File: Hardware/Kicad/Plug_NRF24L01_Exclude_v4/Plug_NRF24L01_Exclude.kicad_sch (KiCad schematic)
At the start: 39 parts, among them J1 Conn_01x07_Socket, J2 Conn_01x08_Socket, J2 Conn_02x07_Odd_Even, Q1 2N7002, Q2 2N7002, Q3 2N7002, SW2 SW_SPST, U2 MIC5219-3.3YMM, U3 STM32L412KBTx

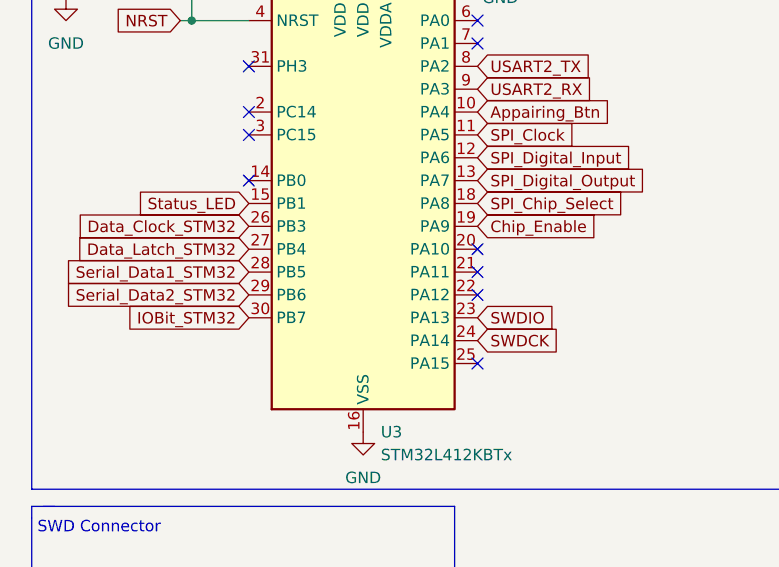
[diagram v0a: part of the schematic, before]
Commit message: Update Plug_NRF24L01_Exclude v4.0a (Schematic Fixes / New PCB Routing) - Added new images
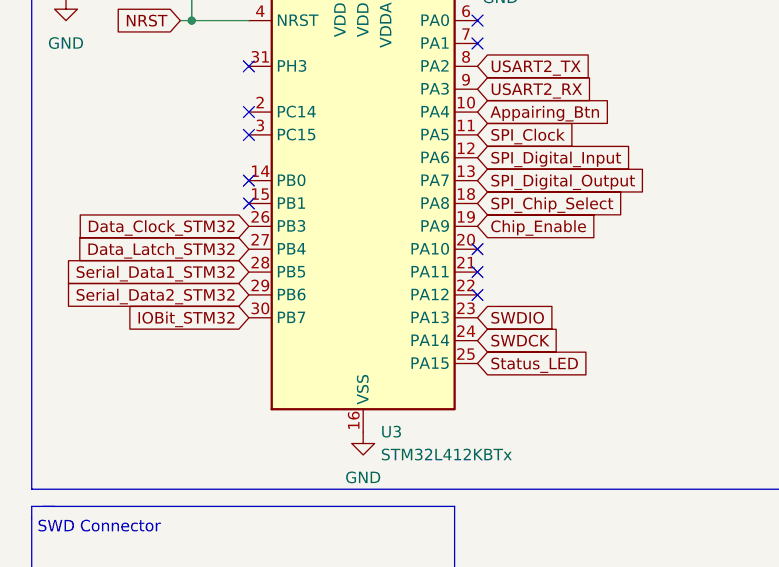
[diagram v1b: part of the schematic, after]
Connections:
- net Status_LED: now also U3.25 (PA15); no longer U3.15 (PB1)
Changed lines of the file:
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@@
     (title "SNES Wireless Receiver (NRF24L01 Exclude)")
     (date "2023-04-20")
-    (rev "3.0d")
+    (rev "4.0a")
     (company "ENSEA")
   )
@@
   (no_connect (at 36.83 121.285))
   (no_connect (at 66.04 39.37))
-  (no_connect (at 66.04 74.93))
   (no_connect (at 66.04 67.31))
   (no_connect (at 40.64 54.61))
+  (no_connect (at 40.64 41.91))
   (no_connect (at 40.64 49.53))
   (no_connect (at 40.64 46.99))
@@
   (no_connect (at 36.83 116.205))
   (no_connect (at 186.055 69.85))
-  (no_connect (at 40.64 41.91))
+  (no_connect (at 40.64 57.15))
   (no_connect (at 66.04 36.83))
   (no_connect (at 49.53 113.665))
@@
     )
   )
+  (global_label "Status_LED" (shape input) (at 66.04 74.93 0) (fields_autoplaced)
+    (effects (font (size 1.27 1.27)) (justify left))
+    (property "Intersheetrefs" "${INTERSHEET_REFS}" (at 79.3475 74.93 0)
+      (effects (font (size 1.27 1.27)) (justify left) hide)
+    )
+  )
   (global_label "SPI_Digital_Output" (shape input) (at 66.04 54.61 0) (fields_autoplaced)
     (effects (font (size 1.27 1.27)) (justify left))
@@
       (effects (font (size 1.27 1.27)) (justify right) hide)
     )
-  )
-  (global_label "Status_LED" (shape input) (at 40.64 57.15 180) (fields_autoplaced)
-    (effects (font (size 1.27 1.27)) (justify right))
-    (property "Intersheetrefs" "${INTERSHEET_REFS}" (at 27.3325 57.15 0)
-      (effects (font (size 1.27 1.27)) (justify right) hide)
-    )
